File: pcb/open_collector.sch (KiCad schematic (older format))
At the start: 24 parts

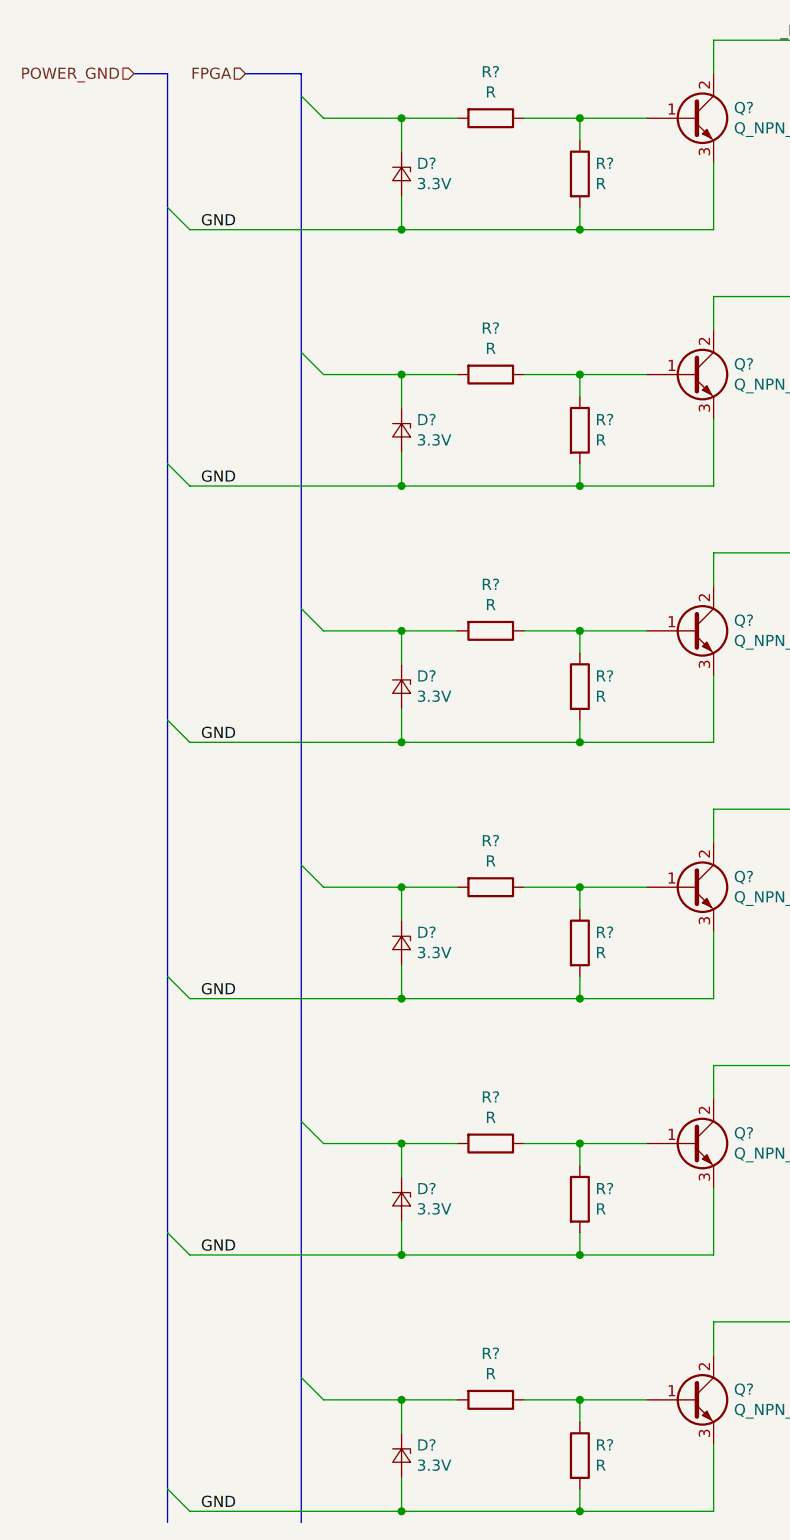
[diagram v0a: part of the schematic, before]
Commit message: FPGA side labels added
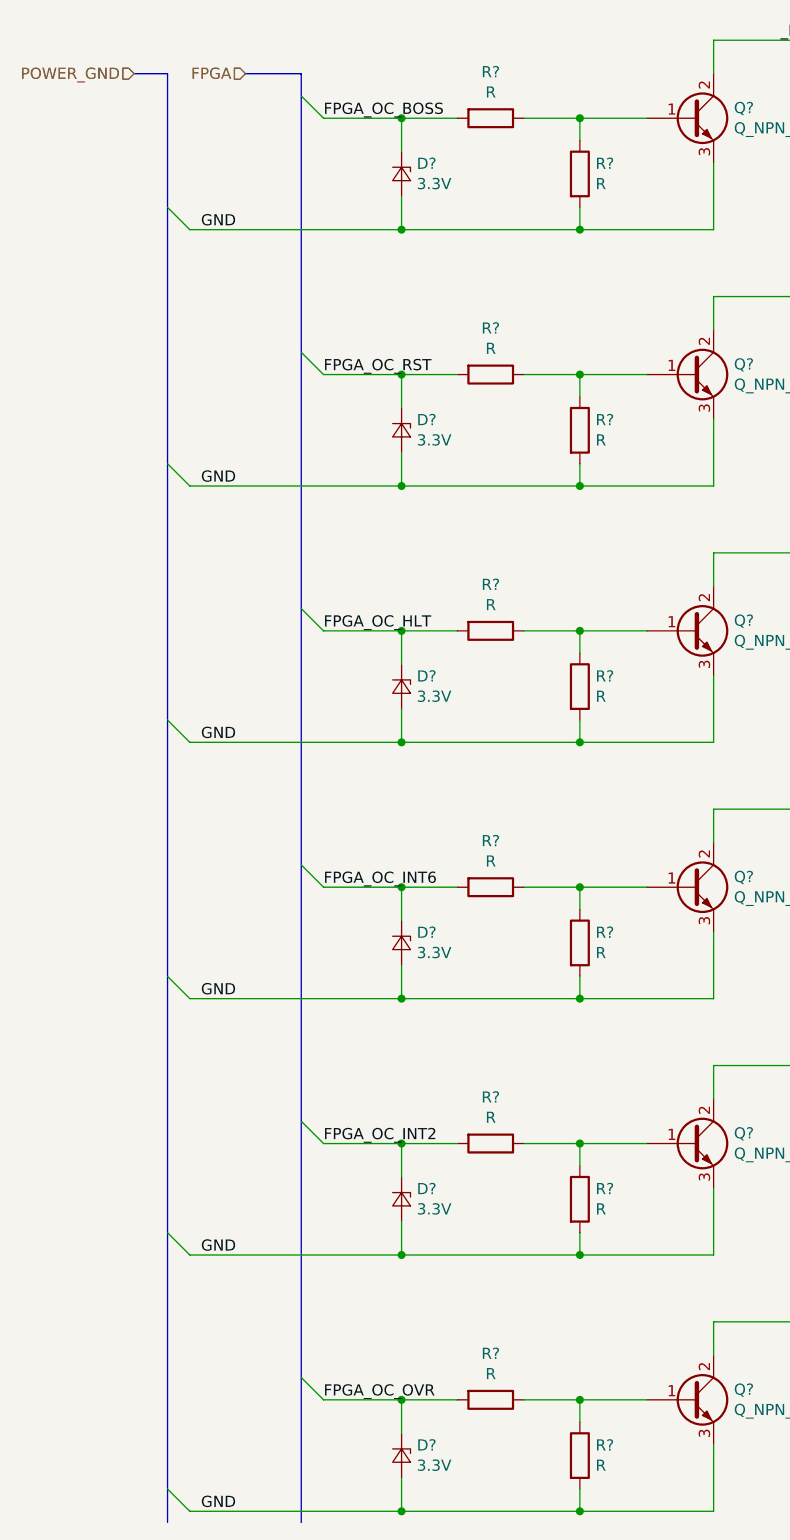
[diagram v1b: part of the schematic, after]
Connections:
- net FPGA_OC_BOSS: now reaches D?.1 (K), R?.2
- net FPGA_OC_RST: now reaches D?.1 (K), R?.2
- net FPGA_OC_HLT: now reaches D?.1 (K), R?.2
- net FPGA_OC_INT6: now reaches D?.1 (K), R?.2
- net FPGA_OC_INT2: now reaches D?.1 (K), R?.2
- net FPGA_OC_OVR: now reaches D?.1 (K), R?.2
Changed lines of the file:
@@
 Wire Bus Line
 	1150 1000 1150 7500
+Text Label 1850 1200 0    50   ~ 0
+FPGA_OC_BOSS
+Text Label 1850 2350 0    50   ~ 0
+FPGA_OC_RST
+Text Label 1850 3500 0    50   ~ 0
+FPGA_OC_HLT
+Text Label 1850 4650 0    50   ~ 0
+FPGA_OC_INT6
+Text Label 1850 5800 0    50   ~ 0
+FPGA_OC_INT2
+Text Label 1850 6950 0    50   ~ 0
+FPGA_OC_OVR
 $EndSCHEMATC

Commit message: Some work done on the whole project
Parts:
- gave numbers to parts that had none: 24
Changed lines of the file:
@@
 FPGA
 $Comp
-L Device:Q_NPN_BCE Q?
+L Device:Q_NPN_BCE Q1
 U 1 1 5EB2F0D3
 P 3500 1200
-F 0 "Q?" H 3691 1246 50  0000 L CNN
+F 0 "Q1" H 3691 1246 50  0000 L CNN
 F 1 "Q_NPN_BCE" H 3691 1155 50  0000 L CNN
 F 2 "" H 3700 1300 50  0001 C CNN
@@
 	1750 1100 1850 1200
 $Comp
-L Device:R R?
+L Device:R R1
 U 1 1 5EB3731B
 P 2600 1200
-F 0 "R?" V 2393 1200 50  0000 C CNN
+F 0 "R1" V 2393 1200 50  0000 C CNN
 F 1 "R" V 2484 1200 50  0000 C CNN
 F 2 "" V 2530 1200 50  0001 C CNN
@@
 	3000 1300 3000 1200
 $Comp
-L Device:R R?
+L Device:R R7
 U 1 1 5EB387D5
 P 3000 1450
-F 0 "R?" H 3070 1496 50  0000 L CNN
+F 0 "R7" H 3070 1496 50  0000 L CNN
 F 1 "R" H 3070 1405 50  0000 L CNN
 F 2 "" V 2930 1450 50  0001 C CNN
@@
 $EndComp
 $Comp
-L Device:D_Zener_Small D?
+L Device:D_Zener_Small D1
 U 1 1 5EB3EBB3
 P 2200 1450
-F 0 "D?" V 2154 1518 50  0000 L CNN
+F 0 "D1" V 2154 1518 50  0000 L CNN
 F 1 "3.3V" V 2245 1518 50  0000 L CNN
 F 2 "" V 2200 1450 50  0001 C CNN
@@
 	2200 1700 1250 1700
 $Comp
-L Device:Q_NPN_BCE Q?
+L Device:Q_NPN_BCE Q2
 U 1 1 5EB4E14D
 P 3500 2350
-F 0 "Q?" H 3691 2396 50  0000 L CNN
+F 0 "Q2" H 3691 2396 50  0000 L CNN
 F 1 "Q_NPN_BCE" H 3691 2305 50  0000 L CNN
 F 2 "" H 3700 2450 50  0001 C CNN
@@
 $EndComp
 $Comp
-L Device:R R?
+L Device:R R2
 U 1 1 5EB4E153
 P 2600 2350
-F 0 "R?" V 2393 2350 50  0000 C CNN
+F 0 "R2" V 2393 2350 50  0000 C CNN
 F 1 "R" V 2484 2350 50  0000 C CNN
 F 2 "" V 2530 2350 50  0001 C CNN
@@
 	3000 2450 3000 2350
 $Comp
-L Device:R R?
+L Device:R R8
 U 1 1 5EB4E160
 P 3000 2600
-F 0 "R?" H 3070 2646 50  0000 L CNN
+F 0 "R8" H 3070 2646 50  0000 L CNN
 F 1 "R" H 3070 2555 50  0000 L CNN
 F 2 "" V 2930 2600 50  0001 C CNN
@@
 $EndComp
 $Comp
-L Device:D_Zener_Small D?
+L Device:D_Zener_Small D2
 U 1 1 5EB4E166
 P 2200 2600
-F 0 "D?" V 2154 2668 50  0000 L CNN
+F 0 "D2" V 2154 2668 50  0000 L CNN
 F 1 "3.3V" V 2245 2668 50  0000 L CNN
 F 2 "" V 2200 2600 50  0001 C CNN
@@
 	2200 2850 1250 2850
 $Comp
-L Device:Q_NPN_BCE Q?
+L Device:Q_NPN_BCE Q3
 U 1 1 5EB5460D
 P 3500 3500
-F 0 "Q?" H 3691 3546 50  0000 L CNN
+F 0 "Q3" H 3691 3546 50  0000 L CNN
 F 1 "Q_NPN_BCE" H 3691 3455 50  0000 L CNN
 F 2 "" H 3700 3600 50  0001 C CNN
@@
 $EndComp
 $Comp
-L Device:R R?
+L Device:R R3
 U 1 1 5EB54613
 P 2600 3500
-F 0 "R?" V 2393 3500 50  0000 C CNN
+F 0 "R3" V 2393 3500 50  0000 C CNN
 F 1 "R" V 2484 3500 50  0000 C CNN
 F 2 "" V 2530 3500 50  0001 C CNN
@@
 	3000 3600 3000 3500
 $Comp
-L Device:R R?
+L Device:R R9
 U 1 1 5EB54620
 P 3000 3750
-F 0 "R?" H 3070 3796 50  0000 L CNN
+F 0 "R9" H 3070 3796 50  0000 L CNN
 F 1 "R" H 3070 3705 50  0000 L CNN
 F 2 "" V 2930 3750 50  0001 C CNN
@@
 $EndComp
 $Comp
-L Device:D_Zener_Small D?
+L Device:D_Zener_Small D3
 U 1 1 5EB54626
 P 2200 3750
-F 0 "D?" V 2154 3818 50  0000 L CNN
+F 0 "D3" V 2154 3818 50  0000 L CNN
 F 1 "3.3V" V 2245 3818 50  0000 L CNN
 F 2 "" V 2200 3750 50  0001 C CNN
@@
 	2200 4000 1250 4000
 $Comp
-L Device:Q_NPN_BCE Q?
+L Device:Q_NPN_BCE Q4
 U 1 1 5EB574A1
 P 3500 4650
-F 0 "Q?" H 3691 4696 50  0000 L CNN
+F 0 "Q4" H 3691 4696 50  0000 L CNN
 F 1 "Q_NPN_BCE" H 3691 4605 50  0000 L CNN
 F 2 "" H 3700 4750 50  0001 C CNN
@@
 $EndComp
 $Comp
-L Device:R R?
+L Device:R R4
 U 1 1 5EB574A7
 P 2600 4650
-F 0 "R?" V 2393 4650 50  0000 C CNN
+F 0 "R4" V 2393 4650 50  0000 C CNN
 F 1 "R" V 2484 4650 50  0000 C CNN
 F 2 "" V 2530 4650 50  0001 C CNN
@@
 	3000 4750 3000 4650
 $Comp
-L Device:R R?
+L Device:R R10
 U 1 1 5EB574B4
 P 3000 4900
-F 0 "R?" H 3070 4946 50  0000 L CNN
+F 0 "R10" H 3070 4946 50  0000 L CNN
 F 1 "R" H 3070 4855 50  0000 L CNN
 F 2 "" V 2930 4900 50  0001 C CNN
@@
 $EndComp
 $Comp
-L Device:D_Zener_Small D?
+L Device:D_Zener_Small D4
 U 1 1 5EB574BA
 P 2200 4900
-F 0 "D?" V 2154 4968 50  0000 L CNN
+F 0 "D4" V 2154 4968 50  0000 L CNN
 F 1 "3.3V" V 2245 4968 50  0000 L CNN
 F 2 "" V 2200 4900 50  0001 C CNN
@@
 	2200 5150 1250 5150
 $Comp
-L Device:Q_NPN_BCE Q?
+L Device:Q_NPN_BCE Q5
 U 1 1 5EB5A30D
 P 3500 5800
-F 0 "Q?" H 3691 5846 50  0000 L CNN
+F 0 "Q5" H 3691 5846 50  0000 L CNN
 F 1 "Q_NPN_BCE" H 3691 5755 50  0000 L CNN
 F 2 "" H 3700 5900 50  0001 C CNN
@@
 $EndComp
 $Comp
-L Device:R R?
+L Device:R R5
 U 1 1 5EB5A313
 P 2600 5800
-F 0 "R?" V 2393 5800 50  0000 C CNN
+F 0 "R5" V 2393 5800 50  0000 C CNN
 F 1 "R" V 2484 5800 50  0000 C CNN
 F 2 "" V 2530 5800 50  0001 C CNN
@@
 	3000 5900 3000 5800
 $Comp
-L Device:R R?
+L Device:R R11
 U 1 1 5EB5A320
 P 3000 6050
-F 0 "R?" H 3070 6096 50  0000 L CNN
+F 0 "R11" H 3070 6096 50  0000 L CNN
 F 1 "R" H 3070 6005 50  0000 L CNN
 F 2 "" V 2930 6050 50  0001 C CNN
@@
 $EndComp
 $Comp
-L Device:D_Zener_Small D?
+L Device:D_Zener_Small D5
 U 1 1 5EB5A326
 P 2200 6050
-F 0 "D?" V 2154 6118 50  0000 L CNN
+F 0 "D5" V 2154 6118 50  0000 L CNN
 F 1 "3.3V" V 2245 6118 50  0000 L CNN
 F 2 "" V 2200 6050 50  0001 C CNN
@@
 	2200 6300 1250 6300
 $Comp
-L Device:Q_NPN_BCE Q?
+L Device:Q_NPN_BCE Q6
 U 1 1 5EB5D15E
 P 3500 6950
-F 0 "Q?" H 3691 6996 50  0000 L CNN
+F 0 "Q6" H 3691 6996 50  0000 L CNN
 F 1 "Q_NPN_BCE" H 3691 6905 50  0000 L CNN
 F 2 "" H 3700 7050 50  0001 C CNN
@@
 $EndComp
 $Comp
-L Device:R R?
+L Device:R R6
 U 1 1 5EB5D164
 P 2600 6950
-F 0 "R?" V 2393 6950 50  0000 C CNN
+F 0 "R6" V 2393 6950 50  0000 C CNN
 F 1 "R" V 2484 6950 50  0000 C CNN
 F 2 "" V 2530 6950 50  0001 C CNN
@@
 	3000 7050 3000 6950
 $Comp
-L Device:R R?
+L Device:R R12
 U 1 1 5EB5D171
 P 3000 7200
-F 0 "R?" H 3070 7246 50  0000 L CNN
+F 0 "R12" H 3070 7246 50  0000 L CNN
 F 1 "R" H 3070 7155 50  0000 L CNN
 F 2 "" V 2930 7200 50  0001 C CNN
@@
 $EndComp
 $Comp
-L Device:D_Zener_Small D?
+L Device:D_Zener_Small D6
 U 1 1 5EB5D177
 P 2200 7200
-F 0 "D?" V 2154 7268 50  0000 L CNN
+F 0 "D6" V 2154 7268 50  0000 L CNN
 F 1 "3.3V" V 2245 7268 50  0000 L CNN
 F 2 "" V 2200 7200 50  0001 C CNN

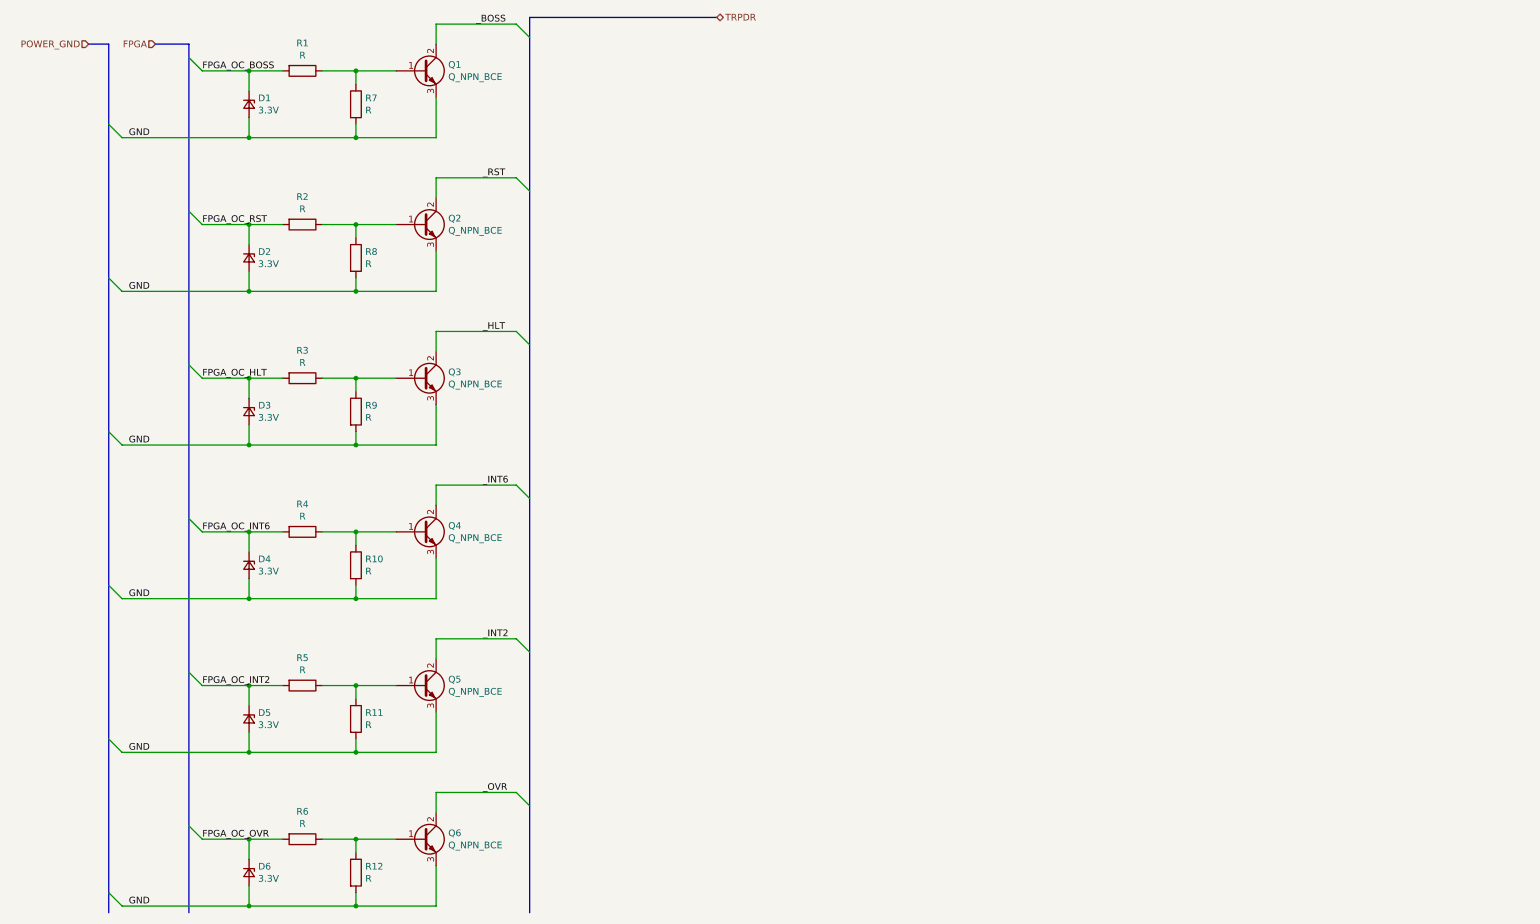
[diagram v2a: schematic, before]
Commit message: ok, we are using global labels now
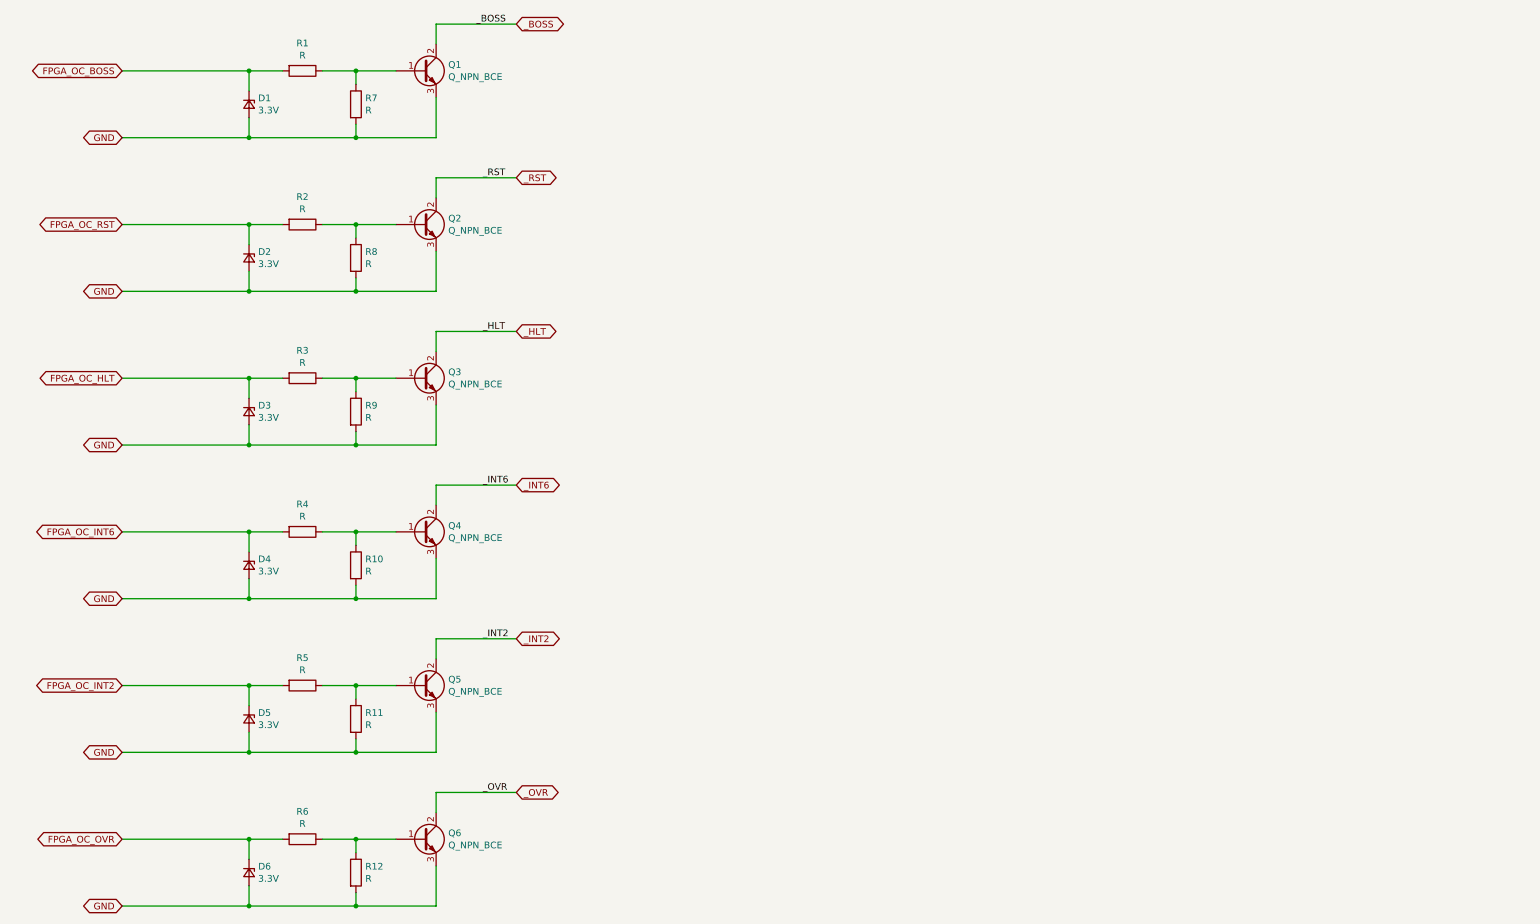
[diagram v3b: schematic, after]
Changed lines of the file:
@@
 $Descr A4 11693 8268
 encoding utf-8
-Sheet 5 11
+Sheet 3 11
 Title "WishMaster 1200"
 Date ""
@@
 Comment4 ""
 $EndDescr
-Text HLabel 1000 1000 0    50   Input ~ 0
-POWER_GND
-Text HLabel 5700 800  2    50   BiDi ~ 0
-TRPDR
-Text HLabel 1500 1000 0    50   Input ~ 0
-FPGA
 $Comp
 L Device:Q_NPN_BCE Q1
@@
 	1    0    0    -1
 $EndComp
-Wire Bus Line
-	1500 1000 1750 1000
-Wire Bus Line
-	1000 1000 1150 1000
-Entry Wire Line
-	1750 1100 1850 1200
 $Comp
 L Device:R R1
@@
 	0    1    1    0
 $EndComp
-Entry Wire Line
-	1150 1600 1250 1700
-Wire Bus Line
-	5700 800  4300 800
 Wire Wire Line
 	3600 1000 3600 850
-Entry Wire Line
-	4200 850  4300 950
 Wire Wire Line
 	3600 1700 3000 1700
@@
 $EndComp
 Wire Wire Line
-	1850 1200 2200 1200
+	1250 1200 2200 1200
 Wire Wire Line
 	4200 850  3600 850
@@
 Wire Wire Line
 	3600 2150 3600 2000
-Entry Wire Line
-	4200 2000 4300 2100
 Wire Wire Line
 	3600 2850 3000 2850
@@
 $EndComp
 Wire Wire Line
-	1850 2350 2200 2350
+	1250 2350 2200 2350
 Wire Wire Line
 	4200 2000 3600 2000
@@
 Wire Wire Line
 	3600 3300 3600 3150
-Entry Wire Line
-	4200 3150 4300 3250
 Wire Wire Line
 	3600 4000 3000 4000
@@
 $EndComp
 Wire Wire Line
-	1850 3500 2200 3500
+	1250 3500 2200 3500
 Wire Wire Line
 	4200 3150 3600 3150
@@
 Wire Wire Line
 	3600 4450 3600 4300
-Entry Wire Line
-	4200 4300 4300 4400
 Wire Wire Line
 	3600 5150 3000 5150
@@
 $EndComp
 Wire Wire Line
-	1850 4650 2200 4650
+	1250 4650 2200 4650
 Wire Wire Line
 	4200 4300 3600 4300
@@
 Wire Wire Line
 	3600 5600 3600 5450
-Entry Wire Line
-	4200 5450 4300 5550
 Wire Wire Line
 	3600 6300 3000 6300
@@
 $EndComp
 Wire Wire Line
-	1850 5800 2200 5800
+	1250 5800 2200 5800
 Wire Wire Line
 	4200 5450 3600 5450
@@
 Wire Wire Line
 	3600 6750 3600 6600
-Entry Wire Line
-	4200 6600 4300 6700
 Wire Wire Line
 	3600 7450 3000 7450
@@
 $EndComp
 Wire Wire Line
-	1850 6950 2200 6950
+	1250 6950 2200 6950
 Wire Wire Line
 	4200 6600 3600 6600
@@
 Wire Wire Line
 	2200 7450 1250 7450
-Text Label 1300 1700 0    50   ~ 0
-GND
 Text Label 3900 850  0    50   ~ 0
 _BOSS
@@
 Text Label 3950 6600 0    50   ~ 0
 _OVR
-Entry Wire Line
-	1750 2250 1850 2350
-Entry Wire Line
-	1150 2750 1250 2850
-Entry Wire Line
-	1750 3400 1850 3500
-Entry Wire Line
-	1150 3900 1250 4000
-Entry Wire Line
-	1750 4550 1850 4650
-Entry Wire Line
-	1150 5050 1250 5150
-Entry Wire Line
-	1750 5700 1850 5800
-Entry Wire Line
-	1150 6200 1250 6300
-Entry Wire Line
-	1750 6850 1850 6950
-Entry Wire Line
-	1150 7350 1250 7450
-Text Label 1300 2850 0    50   ~ 0
+Text GLabel 1250 1700 0    50   BiDi ~ 0
 GND
-Text Label 1300 4000 0    50   ~ 0
+Text GLabel 1250 2850 0    50   BiDi ~ 0
 GND
-Text Label 1300 5150 0    50   ~ 0
+Text GLabel 1250 4000 0    50   BiDi ~ 0
 GND
-Text Label 1300 6300 0    50   ~ 0
+Text GLabel 1250 5150 0    50   BiDi ~ 0
 GND
-Text Label 1300 7450 0    50   ~ 0
+Text GLabel 1250 6300 0    50   BiDi ~ 0
 GND
-Wire Bus Line
-	4300 800  4300 7500
-Wire Bus Line
-	1750 1000 1750 7500
-Wire Bus Line
-	1150 1000 1150 7500
-Text Label 1850 1200 0    50   ~ 0
+Text GLabel 1250 7450 0    50   BiDi ~ 0
+GND
+Text GLabel 1250 1200 0    50   BiDi ~ 0
 FPGA_OC_BOSS
-Text Label 1850 2350 0    50   ~ 0
+Text GLabel 1250 2350 0    50   BiDi ~ 0
 FPGA_OC_RST
-Text Label 1850 3500 0    50   ~ 0
+Text GLabel 1250 3500 0    50   BiDi ~ 0
 FPGA_OC_HLT
-Text Label 1850 4650 0    50   ~ 0
+Text GLabel 1250 4650 0    50   BiDi ~ 0
 FPGA_OC_INT6
-Text Label 1850 5800 0    50   ~ 0
+Text GLabel 1250 5800 0    50   BiDi ~ 0
 FPGA_OC_INT2
-Text Label 1850 6950 0    50   ~ 0
+Text GLabel 1250 6950 0    50   BiDi ~ 0
 FPGA_OC_OVR
+Text GLabel 4200 850  2    50   BiDi ~ 0
+_BOSS
+Text GLabel 4200 2000 2    50   BiDi ~ 0
+_RST
+Text GLabel 4200 3150 2    50   BiDi ~ 0
+_HLT
+Text GLabel 4200 4300 2    50   BiDi ~ 0
+_INT6
+Text GLabel 4200 5450 2    50   BiDi ~ 0
+_INT2
+Text GLabel 4200 6600 2    50   BiDi ~ 0
+_OVR
 $EndSCHEMATC
